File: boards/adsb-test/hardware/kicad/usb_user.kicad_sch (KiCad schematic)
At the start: 0 parts

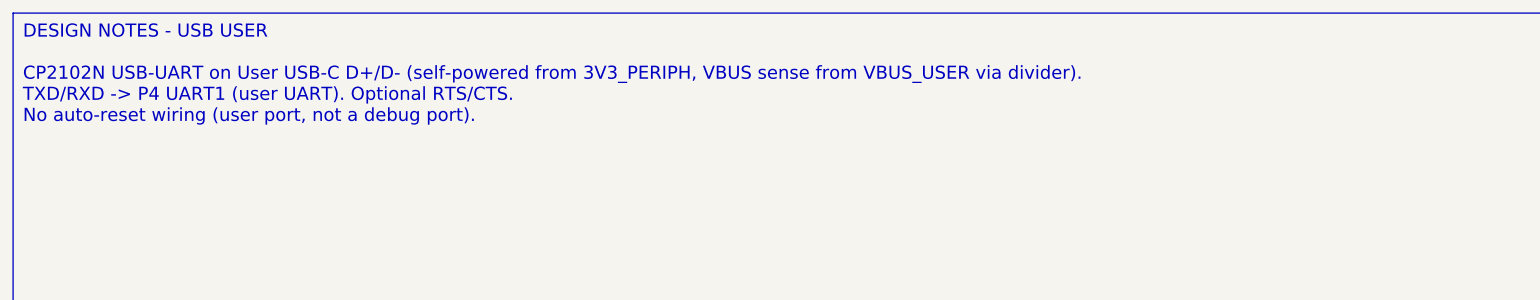
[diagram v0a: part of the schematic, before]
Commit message: Release v0.4.0: ADSB_Test with ESP32-C5, ADSBee m1421 and LA5016 header
- C6 -> C5 co-processor; m1421 identified and integrated (symbol/footprint
  from the ADSBee 1421 carrier, GPL-3.0 attribution)
- Power budget and 2S1P battery sizing for >= 1 h; USB-A for 1-2 SDRs via hub
- Dev port: FT2232H + RP2040 debugprobe; TCA6408A expander for slow I/O
- Test Debug sheet with LA5016 header and rail test points
- Vendor documents git-ignored (public repo)

Co-Authored-By: Claude Opus 5.5 <noreply@anthropic.com>
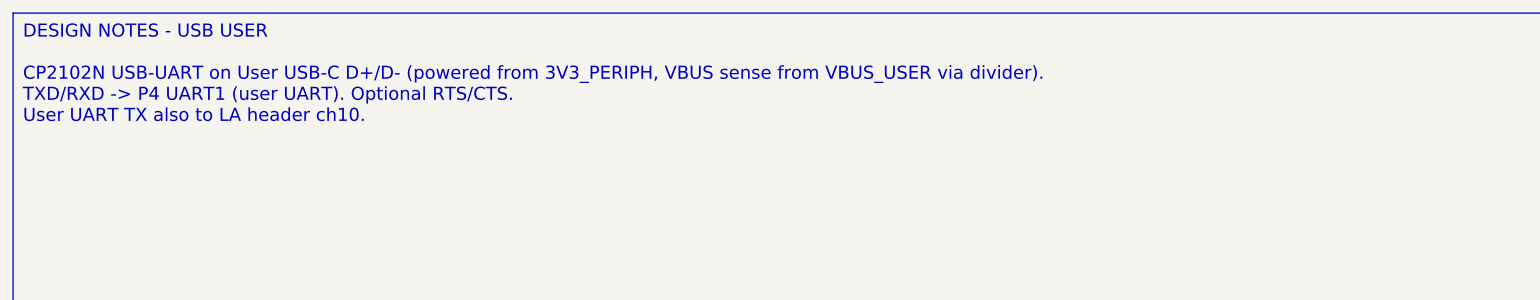
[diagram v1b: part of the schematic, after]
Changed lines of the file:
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@@
 		(comment 1 "Requirements: boards/adsb-test/docs/requirements.md")
 	)
-	(text_box "DESIGN NOTES - USB USER\n\nCP2102N USB-UART on User USB-C D+/D- (self-powered from 3V3_PERIPH, VBUS sense from VBUS_USER via divider).\nTXD/RXD -> P4 UART1 (user UART). Optional RTS/CTS.\nNo auto-reset wiring (user port, not a debug port)."
+	(text_box "DESIGN NOTES - USB USER\n\nCP2102N USB-UART on User USB-C D+/D- (powered from 3V3_PERIPH, VBUS sense from VBUS_USER via divider).\nTXD/RXD -> P4 UART1 (user UART). Optional RTS/CTS.\nUser UART TX also to LA header ch10."
 		(exclude_from_sim no)
 		(at 20 20 0)

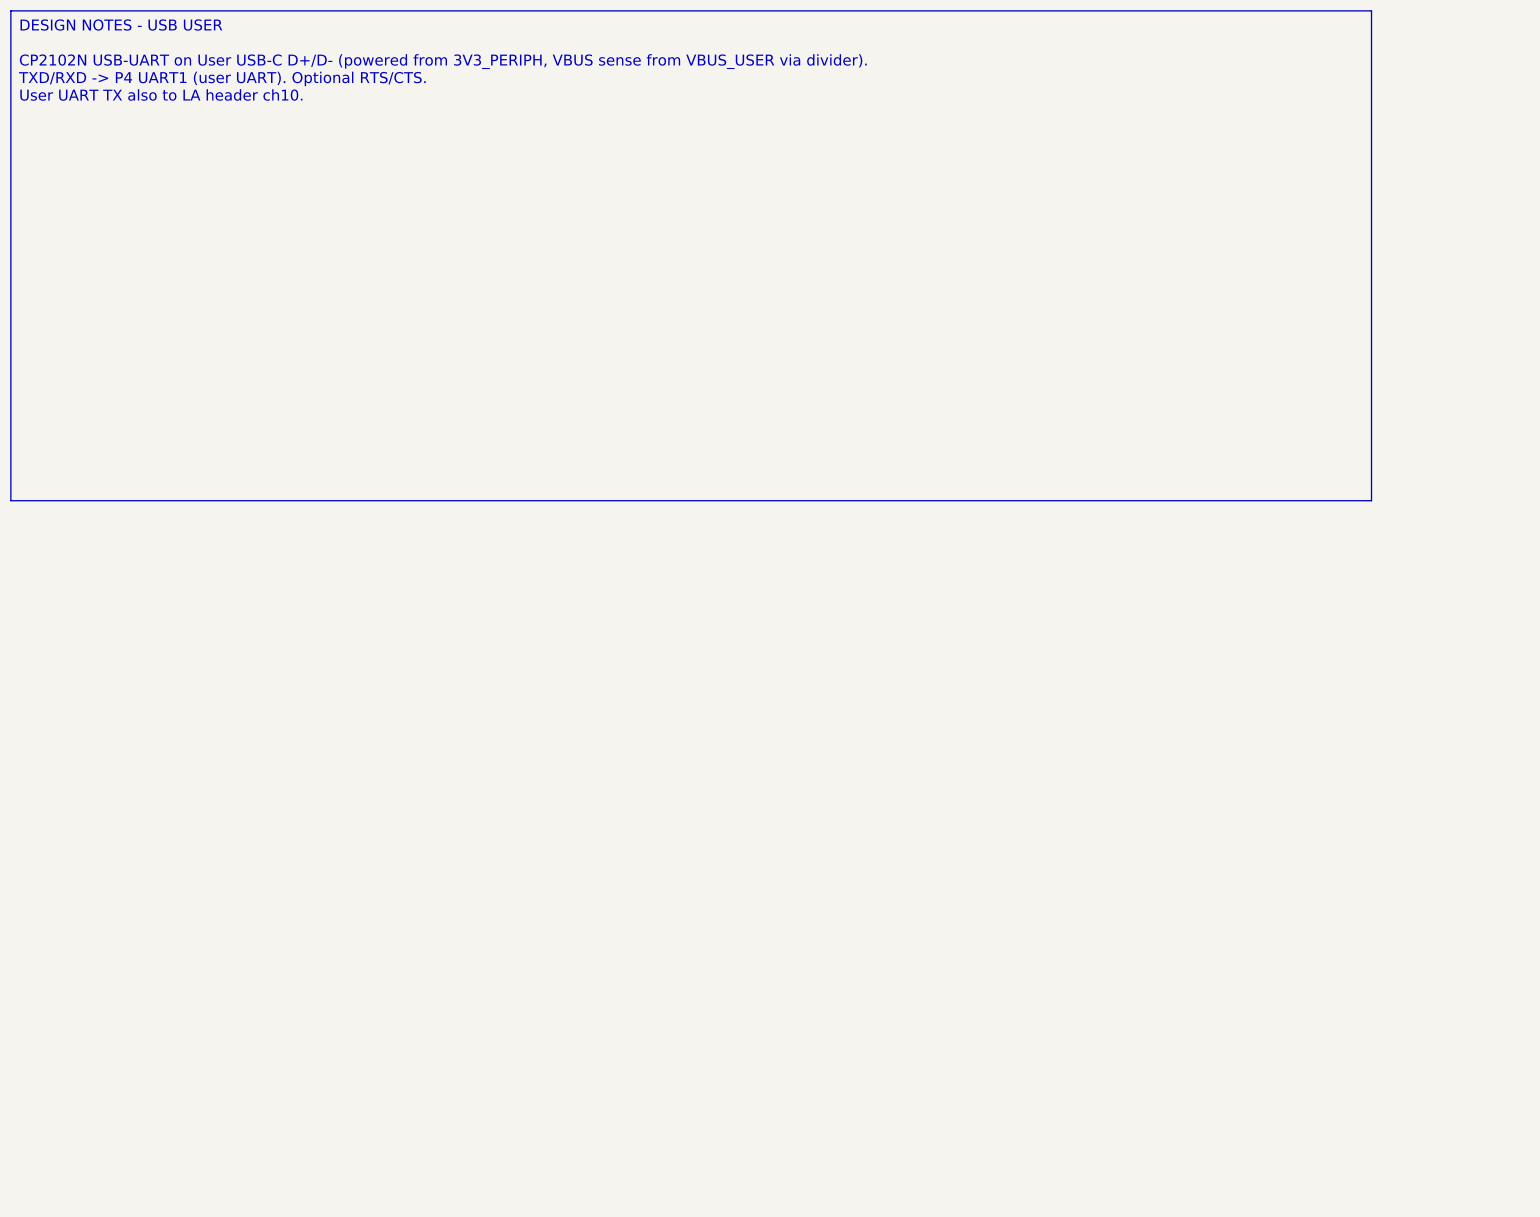
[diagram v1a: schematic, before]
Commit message: Release v0.22.0: all ADSB_Test schematic sheets generated (ERC clean)
Co-Authored-By: Claude Opus 5.5 <noreply@anthropic.com>
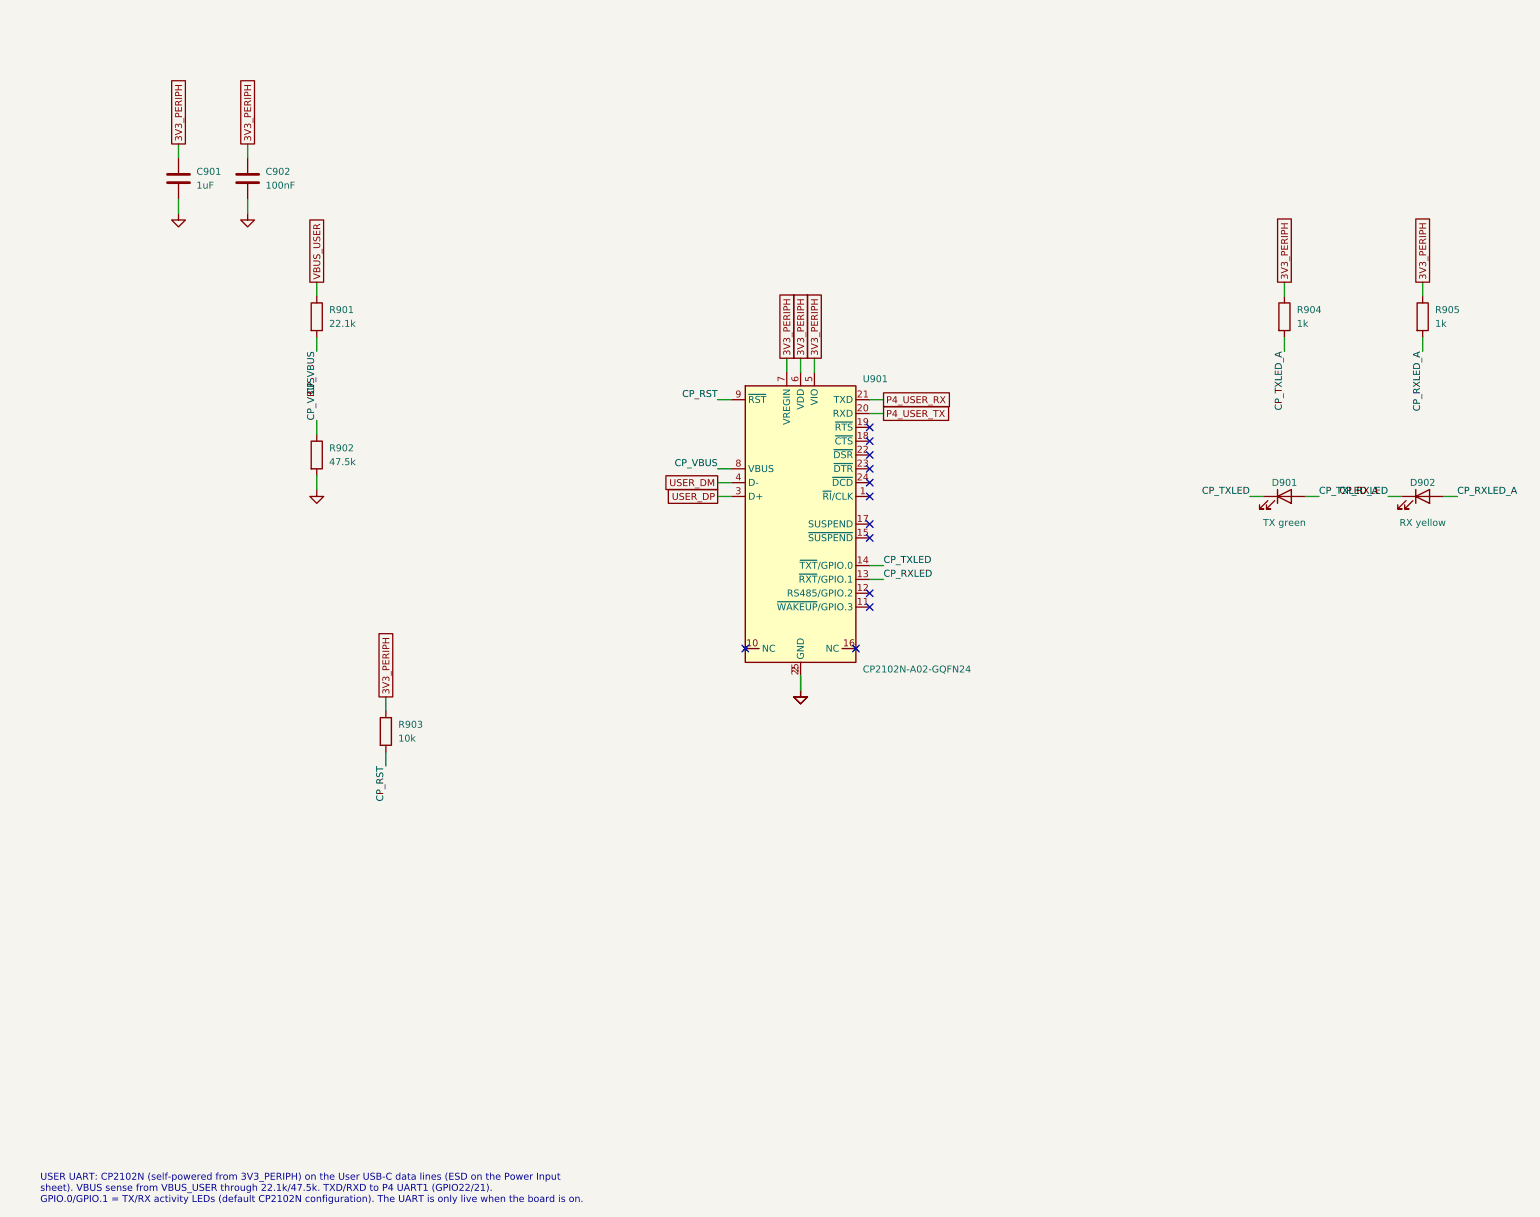
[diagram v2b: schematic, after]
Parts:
- added C901: 1uF, Capacitor_SMD:C_0805_2012Metric_Pad1.18x1.45mm_HandSolder, symbol Device:C
- added C902: 100nF, Capacitor_SMD:C_0805_2012Metric_Pad1.18x1.45mm_HandSolder, symbol Device:C
- added D901: TX green, LED_SMD:LED_0805_2012Metric_Pad1.15x1.40mm_HandSolder, symbol Device:LED
- added D902: RX yellow, LED_SMD:LED_0805_2012Metric_Pad1.15x1.40mm_HandSolder, symbol Device:LED
- added R901: 22.1k, Resistor_SMD:R_0805_2012Metric_Pad1.20x1.40mm_HandSolder, symbol Device:R
- added R902: 47.5k, Resistor_SMD:R_0805_2012Metric_Pad1.20x1.40mm_HandSolder, symbol Device:R
- added R903: 10k, Resistor_SMD:R_0805_2012Metric_Pad1.20x1.40mm_HandSolder, symbol Device:R
- added R904, R905: 1k, Resistor_SMD:R_0805_2012Metric_Pad1.20x1.40mm_HandSolder, symbol Device:R
- added U901: CP2102N-A02-GQFN24, ADSB_Test:QFN-24-1EP_4x4mm_P0.5mm_EP2.6x2.6mm_HandSolder, symbol Interface_USB:CP2102N-Axx-xQFN24
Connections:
- new net 3V3_PERIPH: C901.1, C902.1, R903.1, R904.1, R905.1, U901.5 (VIO), U901.6 (VDD), U901.7 (VREGIN)
- new net CP_RST: R903.2, U901.9 (~{RST})
- new net CP_RXLED: D902.1 (K), U901.13 (~{RXT}/GPIO.1)
- new net CP_RXLED_A: D902.2 (A), R905.2
- new net CP_TXLED: D901.1 (K), U901.14 (~{TXT}/GPIO.0)
- new net CP_TXLED_A: D901.2 (A), R904.2
- new net CP_VBUS: R901.2, R902.1, U901.8 (VBUS)
- new net GND: C901.2, C902.2, R902.2, U901.2 (GND), U901.25 (GND)
- new net P4_USER_RX: U901.21 (TXD)
- new net P4_USER_TX: U901.20 (RXD)
- new net USER_DM: U901.4 (D-)
- new net USER_DP: U901.3 (D+)
- new net VBUS_USER: R901.1
- no-connect marks 0 -> 12
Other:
- note added: "USER UART: CP2102N (self-powered from 3V3_PERIPH) on the User USB-C data lines (ESD on the Power Input sheet). VBUS sense from VBUS_USER through 22.1k/47.5k. TXD/RXD to P4 UART1 (GPIO22/21). GPIO.0/GPIO.1 = TX/RX activity LEDs (default CP2102N configuration). The UART is only live when the board is on."

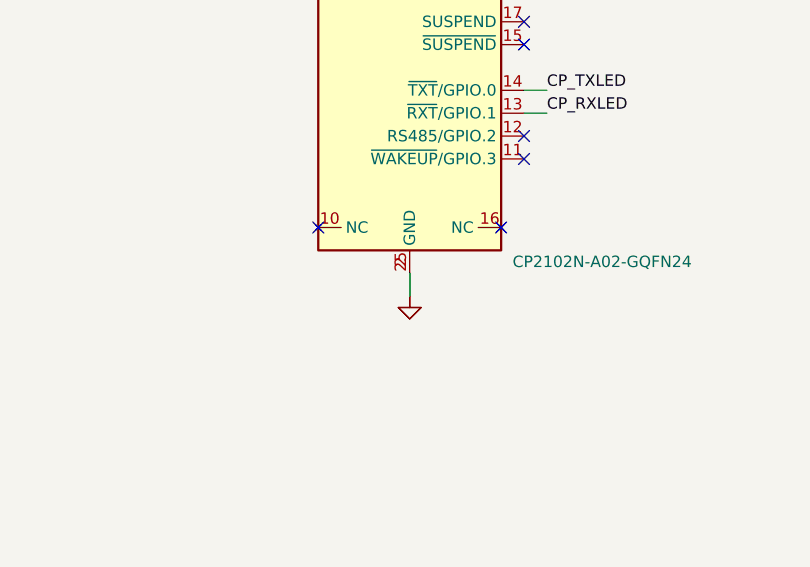
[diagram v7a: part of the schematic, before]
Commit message: Schematic generator: hide stacked pins (KiCad convention) so pin numbers don't overprint
Co-Authored-By: Claude Opus 5.5 <noreply@anthropic.com>
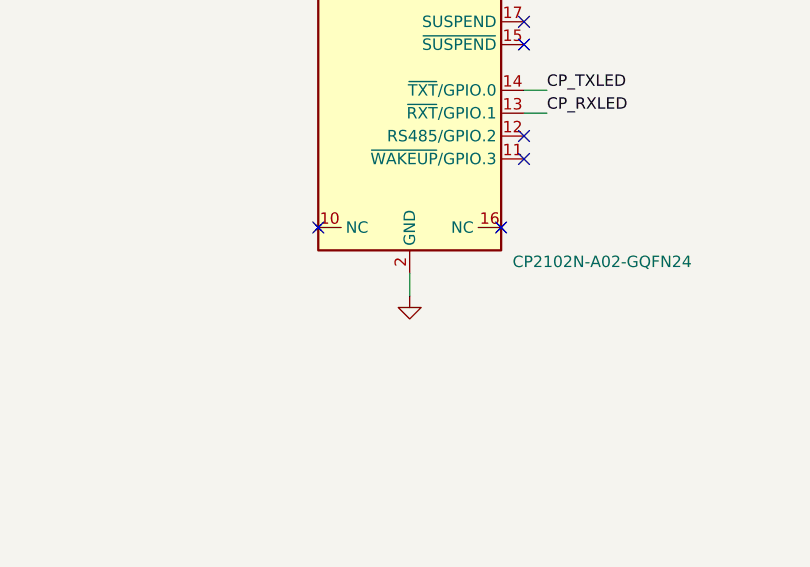
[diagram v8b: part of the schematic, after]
